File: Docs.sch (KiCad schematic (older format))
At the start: 0 parts

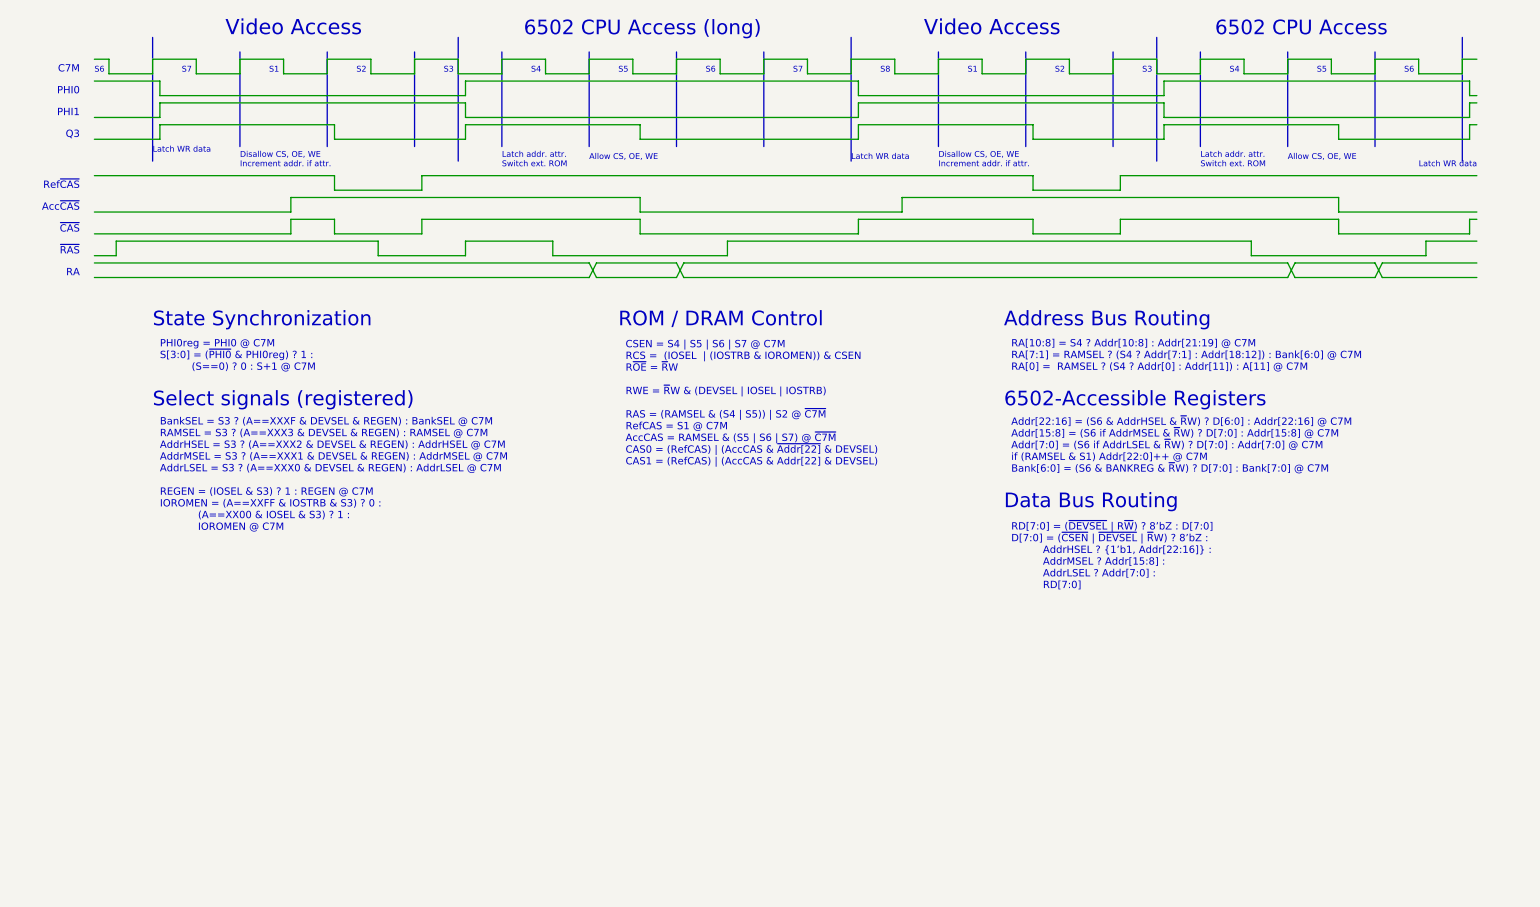
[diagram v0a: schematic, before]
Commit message: CPLD firmware compiles
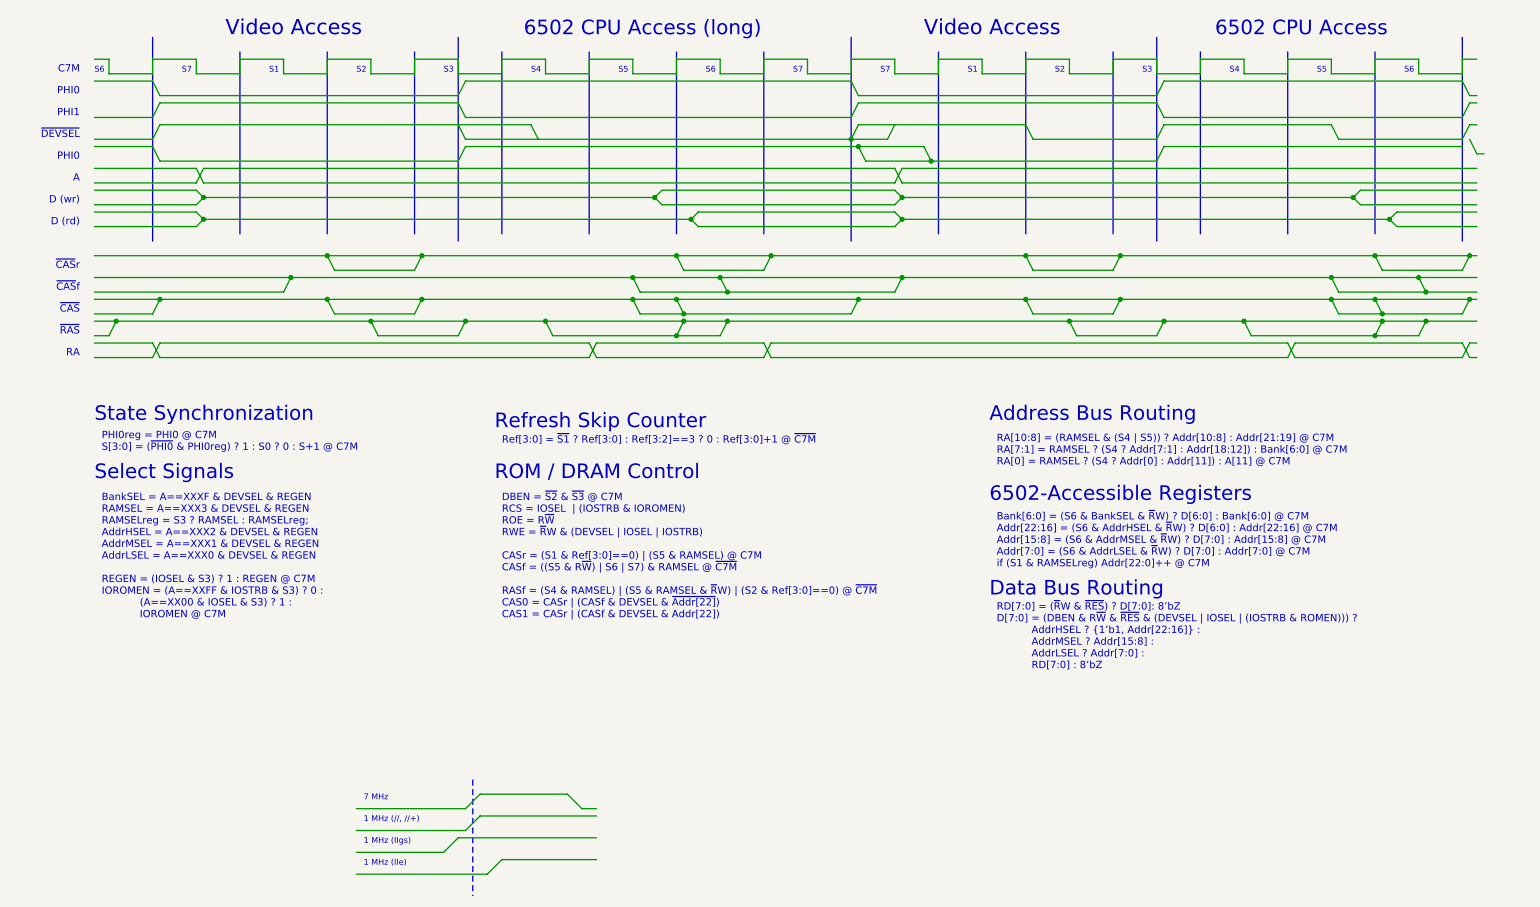
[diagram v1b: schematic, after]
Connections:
- wire segments 176 -> 297
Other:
- note added: "1 MHz (//, //+)"
- note added: "1 MHz (IIe)"
- note added: "1 MHz (IIgs)"
- note added: "7 MHz"
- note added: "A"
- note added: "BankSEL = A==XXXF & DEVSEL & REGEN\nRAMSEL = A==XXX3 & DEVSEL & REGEN\nRAMSELreg = S3 ? RAMSEL : RAMSELreg;\nAddrHSEL = A==XXX2 & DEVSEL & REGEN\nAddrMSEL = A==XXX1 & DEVSEL & REGEN\nAddrLSEL = A==XXX0 & DEVSEL & REGEN\n\nREGEN = (IOSEL & S3) ? 1 : REGEN @ C7M\nIOROMEN = (A==XXFF & IOSTRB & S3) ? 0 :\n (A==XX00 & IOSEL & S3) ? 1 :\n IOROMEN @ C7M"
- note added: "Bank[6:0] = (S6 & BankSEL & ~R~W) ? D[6:0] : Bank[6:0] @ C7M\nAddr[22:16] = (S6 & AddrHSEL & ~R~W) ? D[6:0] : Addr[22:16] @ C7M\nAddr[15:8] = (S6 & AddrMSEL & ~R~W) ? D[7:0] : Addr[15:8] @ C7M\nAddr[7:0] = (S6 & AddrLSEL & ~R~W) ? D[7:0] : Addr[7:0] @ C7M\nif (S1 & RAMSELreg) Addr[22:0]++ @ C7M"
- note added: "D (rd)"
- note added: "D (wr)"
- note added: "DBEN = ~S2~ & ~S3~ @ C7M\nRCS = IOSEL | (IOSTRB & IOROMEN)\nROE = R~W~\nRWE = ~R~W & (DEVSEL | IOSEL | IOSTRB)\n\nCASr = (S1 & Ref[3:0]==0) | (S5 & RAMSEL) @ C7M\nCASf = ((S5 & R~W~) | S6 | S7) & RAMSEL @ ~C7M~\n\nRASf = (S4 & RAMSEL) | (S5 & RAMSEL & ~R~W) | (S2 & Ref[3:0]==0) @ ~C7M~\nCAS0 = CASr | (CASf & DEVSEL & ~Addr[22]~)\nCAS1 = CASr | (CASf & DEVSEL & Addr[22])"
- note added: "PHI0reg = PHI0 @ C7M\nS[3:0] = (~PHI0~ & PHI0reg) ? 1 : S0 ? 0 : S+1 @ C7M"
- note added: "RA[10:8] = (RAMSEL & (S4 | S5)) ? Addr[10:8] : Addr[21:19] @ C7M\nRA[7:1] = RAMSEL ? (S4 ? Addr[7:1] : Addr[18:12]) : Bank[6:0] @ C7M\nRA[0] = RAMSEL ? (S4 ? Addr[0] : Addr[11]) : A[11] @ C7M"
- note added: "RD[7:0] = (~R~W & ~RES~) ? D[7:0]: 8’bZ\nD[7:0] = (DBEN & R~W~ & ~RES~ & (DEVSEL | IOSEL | (IOSTRB & ROMEN))) ?\n AddrHSEL ? {1’b1, Addr[22:16]} : \n AddrMSEL ? Addr[15:8] : \n AddrLSEL ? Addr[7:0] : \n RD[7:0] : 8’bZ"
- note added: "Ref[3:0] = ~S1~ ? Ref[3:0] : Ref[3:2]==3 ? 0 : Ref[3:0]+1 @ ~C7M~"
- note added: "Refresh Skip Counter"
- note added: "Select Signals"
- note added: "~CAS~f"
- note added: "~CAS~r"
- note added: "~DEVSEL~"
- note removed: "Acc~CAS~"
- note removed: "Addr[22:16] = (S6 & AddrHSEL & ~R~W) ? D[6:0] : Addr[22:16] @ C7M\nAddr[15:8] = (S6 if AddrMSEL & ~R~W) ? D[7:0] : Addr[15:8] @ C7M\nAddr[7:0] = (S6 if AddrLSEL & ~R~W) ? D[7:0] : Addr[7:0] @ C7M\nif (RAMSEL & S1) Addr[22:0]++ @ C7M\nBank[6:0] = (S6 & BANKREG & ~R~W) ? D[7:0] : Bank[7:0] @ C7M"
- note removed: "Allow CS, OE, WE"
- note removed: "BankSEL = S3 ? (A==XXXF & DEVSEL & REGEN) : BankSEL @ C7M\nRAMSEL = S3 ? (A==XXX3 & DEVSEL & REGEN) : RAMSEL @ C7M\nAddrHSEL = S3 ? (A==XXX2 & DEVSEL & REGEN) : AddrHSEL @ C7M\nAddrMSEL = S3 ? (A==XXX1 & DEVSEL & REGEN) : AddrMSEL @ C7M\nAddrLSEL = S3 ? (A==XXX0 & DEVSEL & REGEN) : AddrLSEL @ C7M\n\nREGEN = (IOSEL & S3) ? 1 : REGEN @ C7M\nIOROMEN = (A==XXFF & IOSTRB & S3) ? 0 :\n (A==XX00 & IOSEL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"
- note removed: "CSEN = S4 | S5 | S6 | S7 @ C7M\nRCS = (IOSEL | (IOSTRB & IOROMEN)) & CSEN\nR~OE~ = ~R~W\n\nRWE = ~R~W & (DEVSEL | IOSEL | IOSTRB)\n\nRAS = (RAMSEL & (S4 | S5)) | S2 @ ~C7M~\nRefCAS = S1 @ C7M\nAccCAS = RAMSEL & (S5 | S6 | S7) @ ~C7M~\nCAS0 = (RefCAS) | (AccCAS & ~Addr[22]~ & DEVSEL)\nCAS1 = (RefCAS) | (AccCAS & Addr[22] & DEVSEL)"
- note removed: "Disallow CS, OE, WE\nIncrement addr. if attr."
- note removed: "Latch WR data"
- note removed: "Latch addr. attr.\nSwitch ext. ROM"
- note removed: "PHI0reg = PHI0 @ C7M\nS[3:0] = (~PHI0~ & PHI0reg) ? 1 : \n (S==0) ? 0 : S+1 @ C7M"
- note removed: "Q3"
- note removed: "RA[10:8] = S4 ? Addr[10:8] : Addr[21:19] @ C7M\nRA[7:1] = RAMSEL ? (S4 ? Addr[7:1] : Addr[18:12]) : Bank[6:0] @ C7M\nRA[0] = RAMSEL ? (S4 ? Addr[0] : Addr[11]) : A[11] @ C7M"
- note removed: "RD[7:0] = (~DEVSEL~ | R~W~) ? 8’bZ : D[7:0]\nD[7:0] = (~CSEN~ | ~DEVSEL~ | ~R~W) ? 8’bZ :\n AddrHSEL ? {1’b1, Addr[22:16]} : \n AddrMSEL ? Addr[15:8] : \n AddrLSEL ? Addr[7:0] : \n RD[7:0]"
- note removed: "Ref~CAS~"
- note removed: "S8"
- note removed: "Select signals (registered)"
